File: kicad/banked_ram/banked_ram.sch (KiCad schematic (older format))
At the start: 10 parts

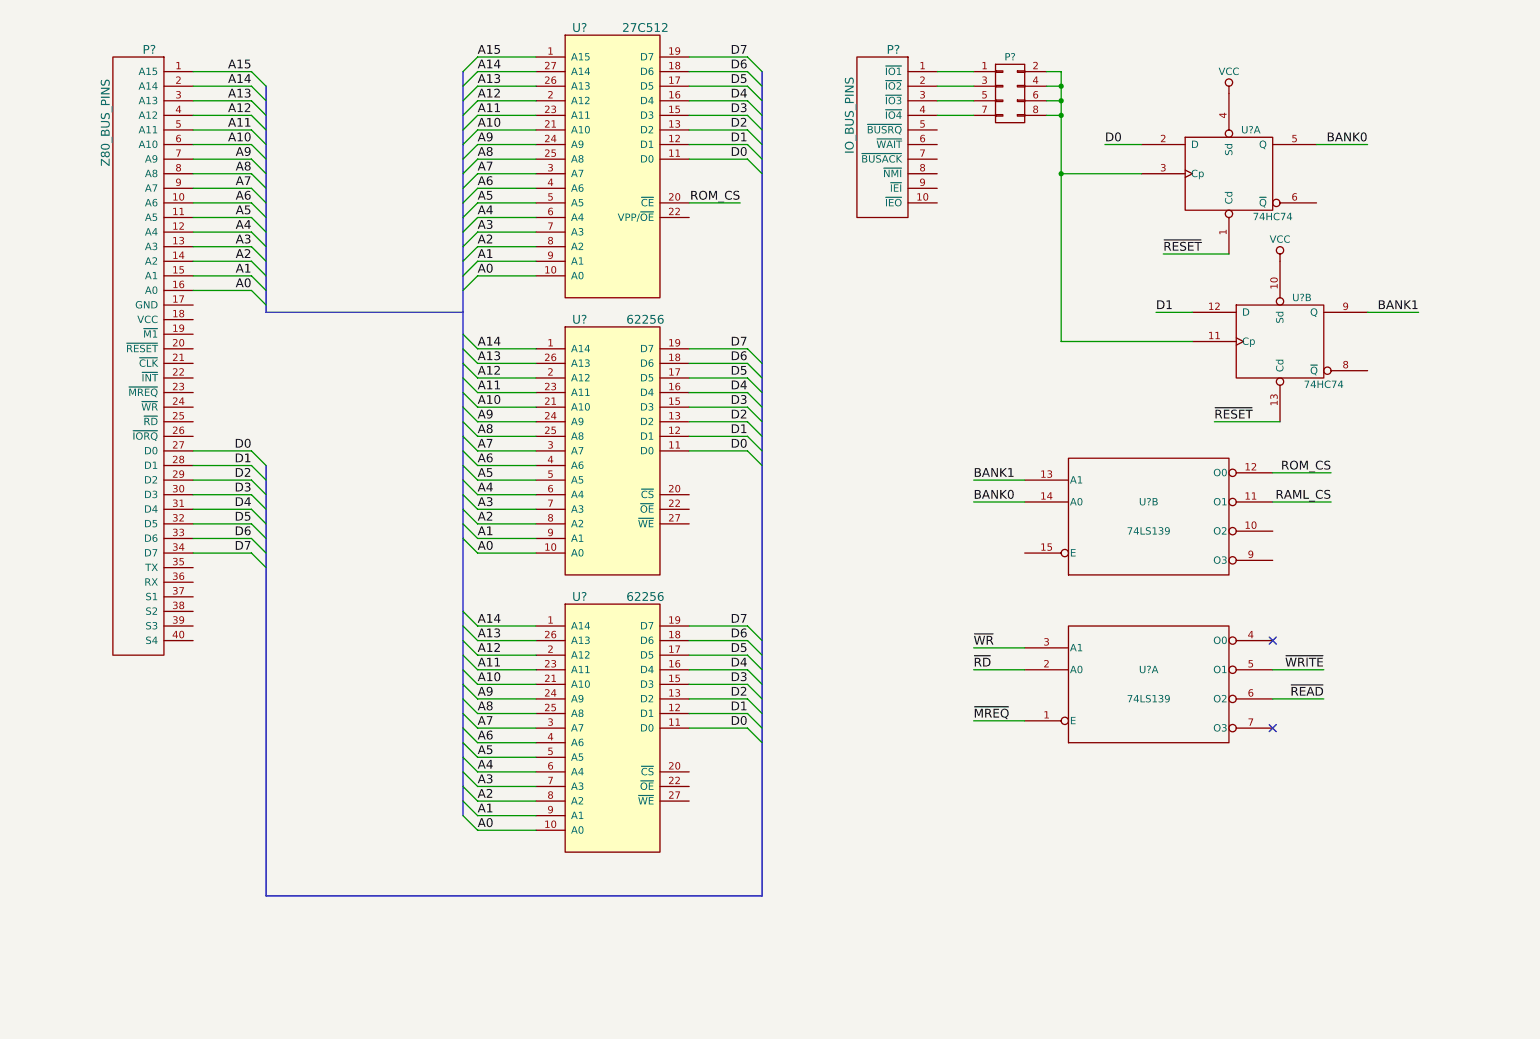
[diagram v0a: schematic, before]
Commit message: Banked RAM board completed
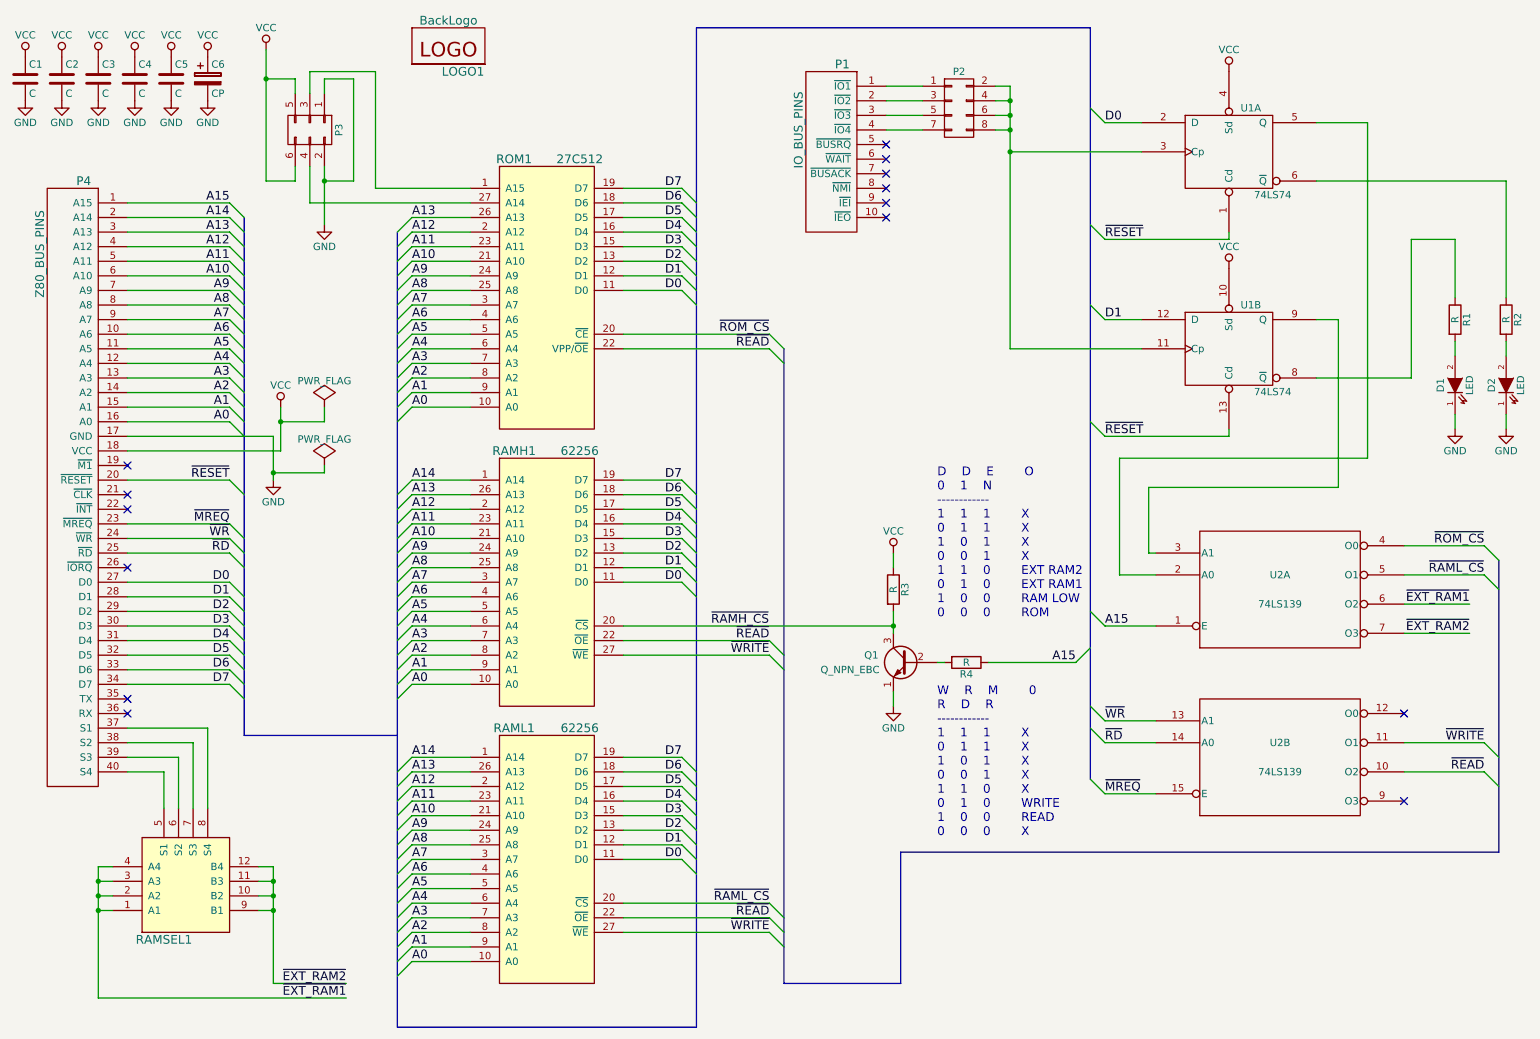
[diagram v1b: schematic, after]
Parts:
- removed U?: 62256, symbol 62256
- removed U? (x2): 74HC74, symbol 74HC74
- added C1, C2, C3, C4, C5: C, Capacitors_ThroughHole:C_Disc_D3_P2.5, symbol C
- added C6: CP, Capacitors_ThroughHole:C_Radial_D5_L11_P2.5, symbol CP
- added D1, D2: LED, LEDs:LED-3MM, symbol LED
- added LOGO1: BackLogo, nrc2016_logo:nrc2016_top_logo_1600, symbol FrontLogo
- added P3: CONN_02X03, Pin_Headers:Pin_Header_Straight_2x03, symbol CONN_02X03
- added Q1: Q_NPN_EBC, TO_SOT_Packages_THT:TO-92_Inline_Narrow_Oval, symbol Q_NPN_EBC
- added R1, R2, R3, R4: R, Resistors_ThroughHole:Resistor_Horizontal_RM10mm, symbol R
- added RAMH1: 62256, Housings_DIP:DIP-28_W15.24mm_LongPads, symbol 62256
- added RAMSEL1: CONN_04x03, nrc2016:ramsel_pins, symbol CONN_04x03
- added U1: 74LS74, Housings_DIP:DIP-14_W7.62mm_LongPads, symbol 74LS74
- P1: renamed from P?; footprint (none) -> nrc2016:Pin_Header_Angled_1x10_nrc2016
- P2: renamed from P?; footprint (none) -> nrc2016:Pin_Header_Straight_2x04_nrc2016
- P4: renamed from P?; footprint (none) -> nrc2016:Pin_Header_Angled_1x40_nrc2016
- RAML1, ROM1: renamed from U?; footprint (none) -> Housings_DIP:DIP-28_W15.24mm_LongPads
- U2: renamed from U?; footprint (none) -> Housings_DIP:DIP-16_W7.62mm_LongPads
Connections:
- net A0: now also RAMH1.10 (A0)
- net A1: now also RAMH1.9 (A1)
- net A10: now also RAMH1.21 (A10)
- net A11: now also RAMH1.23 (A11)
- net A12: now also RAMH1.2 (A12)
- net A13: now also RAMH1.26 (A13)
- net A14: now also RAMH1.1 (A14); no longer ROM1.27 (A14)
- net A15: now also U2.1 (E), R4.1; no longer ROM1.1 (A15)
- net A2: now also RAMH1.8 (A2)
- net A3: now also RAMH1.7 (A3)
- net A4: now also RAMH1.6 (A4)
- net A5: now also RAMH1.5 (A5)
- net A6: now also RAMH1.4 (A6)
- net A7: now also RAMH1.3 (A7)
- net A8: now also RAMH1.25 (A8)
- net A9: now also RAMH1.24 (A9)
- net D0: now also RAMH1.11 (D0), U1.2 (D)
- net D1: now also RAMH1.12 (D1), U1.12 (D)
- net D2: now also RAMH1.13 (D2)
- net D3: now also RAMH1.15 (D3)
- net D4: now also RAMH1.16 (D4)
- net D5: now also RAMH1.17 (D5)
- net D6: now also RAMH1.18 (D6)
- net D7: now also RAMH1.19 (D7)
- net GND: now also P4.17 (GND), C1.2, C2.2, C3.2, C4.2, C5.2, C6.2, D1.1 (K), D2.1 (K), P3.1 (P1), P3.2 (P2), Q1.1 (E), RAMH1.14 (GND), U1.7 (GND), U1.7 (GND)
- net VCC: now also P4.18 (VCC), C1.1, C2.1, C3.1, C4.1, C5.1, C6.1, P3.5 (P5), P3.6 (P6), R3.1, RAMH1.28 (VCC), U1.10 (Sd), U1.14 (VCC), U1.14 (VCC), U1.4 (Sd)
- net ~MREQ: now also P4.23 (~MREQ), U2.15 (E); no longer U2.1 (E)
- net ~RD: now also P4.25 (~RD), U2.14 (A0); no longer U2.2 (A0)
- net ~READ: now also RAML1.22 (~OE), ROM1.22 (VPP/~OE), U2.10 (O2), RAMH1.22 (~OE); no longer U2.6 (O2)
- net ~RESET: now also P4.20 (~RESET), U1.1 (Cd), U1.13 (Cd)
- net ~WR: now also P4.24 (~WR), U2.13 (A1); no longer U2.3 (A1)
- net ~WRITE: now also RAML1.27 (~WE), U2.11 (O1), RAMH1.27 (~WE); no longer U2.5 (O1)
- net ~RAML_CS: now reaches RAML1.20 (~CS)
- net ~RAML_CS: now also U2.5 (O1)
- net at P4.37 (S1): now also RAMSEL1.8 (S4)
- net at P4.38 (S2): now also RAMSEL1.7 (S3)
- net at P4.39 (S3): now also RAMSEL1.6 (S2)
- net at P4.40 (S4): now also RAMSEL1.5 (S1)
- net at P2.2 (P2), P2.4 (P4), P2.6 (P6)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: now also U1.11 (Cp), U1.3 (Cp)
- removed net BANK0: U2.14 (A0)
- removed net BANK1: U2.13 (A1)
- removed net RAML_CS: U2.11 (O1)
- net ROM_CS renamed ~ROM_CS
- net ~ROM_CS: now also U2.4 (O0); no longer U2.12 (O0)
- new net: P3.3 (P3), ROM1.1 (A15)
- new net: P3.4 (P4), ROM1.27 (A14)
- new net: U1.5 (Q), U2.2 (A0)
- new net: U1.9 (Q), U2.3 (A1)
- new net: R2.1, U1.6 (~Q)
- new net: R1.1, U1.8 (~Q)
- new net: Q1.2 (B), R4.2
- new net: D1.2 (A), R1.2
- new net: D2.2 (A), R2.2
- new net ~EXT_RAM1: RAMSEL1.1 (A1), RAMSEL1.2 (A2), RAMSEL1.3 (A3), RAMSEL1.4 (A4), U2.6 (O2)
- new net ~EXT_RAM2: RAMSEL1.10 (B2), RAMSEL1.11 (B3), RAMSEL1.12 (B4), RAMSEL1.9 (B1), U2.7 (O3)
- new net ~RAMH_CS: Q1.3 (C), R3.2, RAMH1.20 (~CS)
- no-connect marks 2 -> 14
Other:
- note added: "D D E O\n0 1 N \n------------\n1 1 1 X\n0 1 1 X\n1 0 1 X\n0 0 1 X\n1 1 0 EXT RAM2\n0 1 0 EXT RAM1\n1 0 0 RAM LOW\n0 0 0 ROM\n"
- note added: "W R M 0\nR D R\n------------\n1 1 1 X\n0 1 1 X\n1 0 1 X\n0 0 1 X\n1 1 0 X\n0 1 0 WRITE\n1 0 0 READ\n0 0 0 X"
- moved on the sheet: P1, P2, P4, RAML1, ROM1
